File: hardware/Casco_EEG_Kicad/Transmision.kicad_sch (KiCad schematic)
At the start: 9 parts, among them U2 HC-05

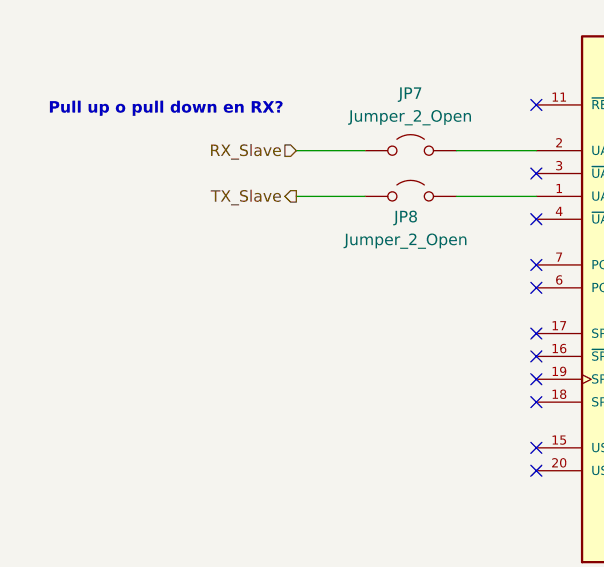
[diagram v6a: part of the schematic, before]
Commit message: Agrego GND para puente UART al modulo BT
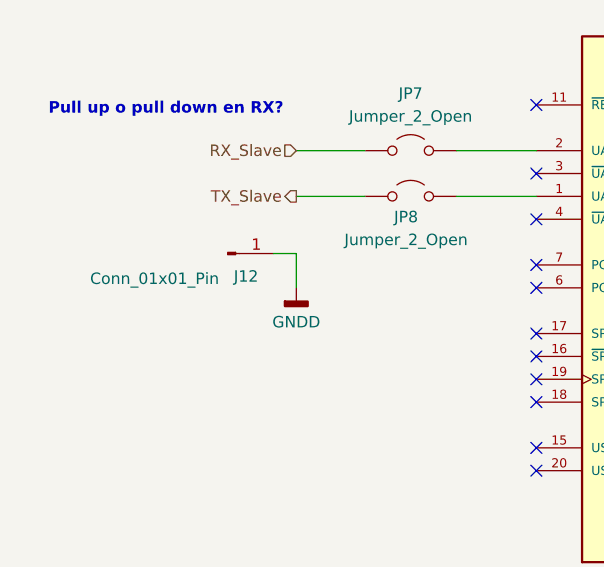
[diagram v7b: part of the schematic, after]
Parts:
- added J12: Conn_01x01_Pin, Connector_PinHeader_2.54mm:PinHeader_1x01_P2.54mm_Vertical, symbol Connector:Conn_01x01_Pin
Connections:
- net GNDD: now also J12.1 (Pin_1)
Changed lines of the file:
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@@
+	(wire
+		(pts
+			(xy 87.63 80.01) (xy 85.09 80.01)
+		)
+		(stroke
+			(width 0)
+			(type default)
+		)
+	)
 	(wire
 		(pts
@@
 		(pts
 			(xy 154.94 91.44) (xy 167.64 91.44)
+		)
+		(stroke
+			(width 0)
+			(type default)
+		)
+	)
+	(wire
+		(pts
+			(xy 87.63 83.82) (xy 87.63 80.01)
 		)
 		(stroke
@@
 	)
 	(symbol
+		(lib_id "Connector:Conn_01x01_Pin")
+		(at 80.01 80.01 0)
+		(unit 1)
+		(exclude_from_sim no)
+		(in_bom yes)
+		(on_board yes)
+		(dnp no)
+		(property "Reference" "J12"
+			(at 82.042 82.55 0)
+			(effects
+				(font
+					(size 1.27 1.27)
+				)
+			)
+		)
+		(property "Value" "Conn_01x01_Pin"
+			(at 71.882 82.804 0)
+			(effects
+				(font
+					(size 1.27 1.27)
+				)
+			)
+		)
+		(property "Footprint" "Connector_PinHeader_2.54mm:PinHeader_1x01_P2.54mm_Vertical"
+			(at 80.01 80.01 0)
+			(effects
+				(font
+					(size 1.27 1.27)
+				)
+				(hide yes)
+			)
+		)
+		(property "Datasheet" "~"
+			(at 80.01 80.01 0)
+			(effects
+				(font
+					(size 1.27 1.27)
+				)
+				(hide yes)
+			)
+		)
+		(property "Description" "Generic connector, single row, 01x01, script generated"
+			(at 80.01 80.01 0)
+			(effects
+				(font
+					(size 1.27 1.27)
+				)
+				(hide yes)
+			)
+		)
+		(pin "1"
+		)
+		(instances
+			(project ""
+				(path "/3414db36-80da-469c-8b48-81d6bd2f8966/fe171ca0-0165-4621-a7c1-0aa23dfd8c22"
+					(reference "J12")
+					(unit 1)
+				)
+			)
+		)
+	)
+	(symbol
 		(lib_id "Device:LED")
 		(at 180.34 83.82 180)
@@
 					(unit 1)
 				)
+			)
+		)
+	)
+	(symbol
+		(lib_id "power:GNDD")
+		(at 87.63 83.82 0)
+		(unit 1)
+		(exclude_from_sim no)
+		(in_bom yes)
+		(on_board yes)
+		(dnp no)
+		(fields_autoplaced yes)
+		(property "Reference" "#PWR054"
+			(at 87.63 90.17 0)
+			(effects
+				(font
+					(size 1.27 1.27)
+				)
+				(hide yes)
+			)
+		)
+		(property "Value" "GNDD"
+			(at 87.63 87.63 0)
+			(effects
+				(font
+					(size 1.27 1.27)
+				)
+			)
+		)
+		(property "Footprint" ""
+			(at 87.63 83.82 0)
+			(effects
+				(font
+					(size 1.27 1.27)
+				)
+				(hide yes)
+			)
+		)
+		(property "Datasheet" ""
+			(at 87.63 83.82 0)
+			(effects
+				(font
+					(size 1.27 1.27)
+				)
+				(hide yes)
+			)
+		)
+		(property "Description" "Power symbol creates a global label with name \"GNDD\" , digital ground"
+			(at 87.63 83.82 0)
+			(effects
+				(font
+					(size 1.27 1.27)
+				)
+				(hide yes)
+			)
+		)
+		(pin "1"
+		)
+		(instances
+			(project "Casco_EEG_Kicad"
+				(path "/3414db36-80da-469c-8b48-81d6bd2f8966/fe171ca0-0165-4621-a7c1-0aa23dfd8c22"
+					(reference "#PWR054")
+					(unit 1)
+				)
